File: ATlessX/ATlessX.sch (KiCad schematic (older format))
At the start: 13 parts, among them U1 74LS74, U2 74LS14

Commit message: More of the circuit done
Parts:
- gave numbers to parts that had none: 1
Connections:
- wire segments 12 -> 31
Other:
- moved on the sheet: C?, SW?, U2A
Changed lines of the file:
@@
 $Comp
 L 74xx:74LS14 U2
-U 1 1 5DD82518
-P 2500 2300
-F 0 "U2" H 2500 2617 50  0000 C CNN
-F 1 "74LS14" H 2500 2526 50  0000 C CNN
-F 2 "" H 2500 2300 50  0001 C CNN
-F 3 "http://www.ti.com/lit/gpn/sn74LS14" H 2500 2300 50  0001 C CNN
-	1    2500 2300
+U 2 1 5DD82518
+P 2650 3500
+F 0 "U2" H 2650 3817 50  0000 C CNN
+F 1 "74LS14" H 2650 3726 50  0000 C CNN
+F 2 "" H 2650 3500 50  0001 C CNN
+F 3 "http://www.ti.com/lit/gpn/sn74LS14" H 2650 3500 50  0001 C CNN
+	2    2650 3500
 	1    0    0    -1
 $EndComp
@@
 L Switch:SW_Push SW?
 U 1 1 5DD82728
-P 2250 3600
-F 0 "SW?" H 2250 3885 50  0000 C CNN
-F 1 "SW_Push" H 2250 3794 50  0000 C CNN
-F 2 "" H 2250 3800 50  0001 C CNN
-F 3 "~" H 2250 3800 50  0001 C CNN
-	1    2250 3600
-	1    0    0    -1
+P 850 3950
+F 0 "SW?" V 896 3902 50  0000 R CNN
+F 1 "SW_Push" V 805 3902 50  0000 R CNN
+F 2 "" H 850 4150 50  0001 C CNN
+F 3 "~" H 850 4150 50  0001 C CNN
+	1    850  3950
+	0    -1   -1   0
 $EndComp
 $Comp
 L Device:CP1_Small C?
 U 1 1 5DD82992
-P 2150 4400
-F 0 "C?" H 2241 4446 50  0000 L CNN
-F 1 "CP1_Small" H 2241 4355 50  0000 L CNN
-F 2 "" H 2150 4400 50  0001 C CNN
-F 3 "~" H 2150 4400 50  0001 C CNN
-	1    2150 4400
-	1    0    0    -1
-$EndComp
-$Comp
-L 74xx:74LS14 U?
+P 1950 4050
+F 0 "C?" H 2041 4096 50  0000 L CNN
+F 1 "CP1_Small" H 2041 4005 50  0000 L CNN
+F 2 "" H 1950 4050 50  0001 C CNN
+F 3 "~" H 1950 4050 50  0001 C CNN
+	1    1950 4050
+	1    0    0    -1
+$EndComp
+$Comp
+L 74xx:74LS14 U2
 U 1 1 5DD82CD4
-P 2900 1900
-F 0 "U?" H 2900 2217 50  0000 C CNN
-F 1 "74LS14" H 2900 2126 50  0000 C CNN
-F 2 "" H 2900 1900 50  0001 C CNN
-F 3 "http://www.ti.com/lit/gpn/sn74LS14" H 2900 1900 50  0001 C CNN
-	1    2900 1900
-	1    0    0    -1
-$EndComp
-$Comp
-L 74xx:74LS14 U?
-U 1 1 5DD82D12
-P 3250 2350
-F 0 "U?" H 3250 2667 50  0000 C CNN
-F 1 "74LS14" H 3250 2576 50  0000 C CNN
-F 2 "" H 3250 2350 50  0001 C CNN
-F 3 "http://www.ti.com/lit/gpn/sn74LS14" H 3250 2350 50  0001 C CNN
-	1    3250 2350
+P 3250 2850
+F 0 "U2" H 3250 3167 50  0000 C CNN
+F 1 "74LS14" H 3250 3076 50  0000 C CNN
+F 2 "" H 3250 2850 50  0001 C CNN
+F 3 "http://www.ti.com/lit/gpn/sn74LS14" H 3250 2850 50  0001 C CNN
+	1    3250 2850
+	1    0    0    -1
+$EndComp
+$Comp
+L 74xx:74LS14 U2
+U 3 1 5DD82D12
+P 3800 3500
+F 0 "U2" H 3800 3817 50  0000 C CNN
+F 1 "74LS14" H 3800 3726 50  0000 C CNN
+F 2 "" H 3800 3500 50  0001 C CNN
+F 3 "http://www.ti.com/lit/gpn/sn74LS14" H 3800 3500 50  0001 C CNN
+	3    3800 3500
 	1    0    0    -1
 $EndComp
@@
 L Device:CP1_Small C?
 U 1 1 5DD82E48
-P 1700 3950
-F 0 "C?" H 1791 3996 50  0000 L CNN
-F 1 "CP1_Small" H 1791 3905 50  0000 L CNN
-F 2 "" H 1700 3950 50  0001 C CNN
-F 3 "~" H 1700 3950 50  0001 C CNN
-	1    1700 3950
-	1    0    0    -1
-$EndComp
+P 1350 4050
+F 0 "C?" H 1441 4096 50  0000 L CNN
+F 1 "CP1_Small" H 1441 4005 50  0000 L CNN
+F 2 "" H 1350 4050 50  0001 C CNN
+F 3 "~" H 1350 4050 50  0001 C CNN
+	1    1350 4050
+	1    0    0    -1
+$EndComp
+Wire Wire Line
+	2950 3500 3500 3500
+Wire Wire Line
+	4100 3500 5100 3500
+Wire Wire Line
+	5100 3500 5100 2500
+Wire Wire Line
+	5100 2500 5700 2500
+Wire Wire Line
+	5700 2500 5700 2850
+Wire Wire Line
+	3550 2850 4700 2850
+Wire Wire Line
+	4700 2850 4700 3150
+Wire Wire Line
+	4700 3150 5400 3150
+Wire Wire Line
+	5400 3050 5250 3050
+Wire Wire Line
+	5250 3050 5250 3700
+Wire Wire Line
+	5250 3700 6200 3700
+Wire Wire Line
+	6200 3700 6200 3250
+Wire Wire Line
+	6200 3250 6000 3250
+Wire Wire Line
+	850  4150 850  4450
+Wire Wire Line
+	850  4450 1350 4450
+Wire Wire Line
+	1950 4450 1950 4150
+Wire Wire Line
+	1350 4150 1350 4450
+Connection ~ 1350 4450
+Wire Wire Line
+	1350 4450 1950 4450
+$Comp
+L power:GND #PWR?
+U 1 1 5DD84F2D
+P 1350 4750
+F 0 "#PWR?" H 1350 4500 50  0001 C CNN
+F 1 "GND" V 1355 4622 50  0000 R CNN
+F 2 "" H 1350 4750 50  0001 C CNN
+F 3 "" H 1350 4750 50  0001 C CNN
+	1    1350 4750
+	1    0    0    -1
+$EndComp
+Wire Wire Line
+	1350 4450 1350 4750
 $EndSCHEMATC

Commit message: Update schematic
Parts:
- C1: renamed from C?; value CP1_Small -> 1uF
- C2: renamed from C?; value CP1_Small -> 10uF
- D1, D2: renamed from D?; value D_Small -> 1N4148
- R1, R2: renamed from R?; value R_Small -> 10K
- R3: renamed from R?; value R_Small -> 470
- SW1: renamed from SW?; value SW_Push -> Power
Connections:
- net labels added: 5VSB, PWR_SW
- wire segments 31 -> 51
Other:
- note added: "ATX Power On Circuit"
- moved on the sheet: D1, D2, R1, R2, R3
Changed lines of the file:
@@
 F 3 "74xx/74hc_hct74.pdf" H 5600 1250 50  0001 C CNN
 	3    5600 1250
-	0    1    1    0
+	0    -1   1    0
 $EndComp
 $Comp
@@
 F 3 "http://www.ti.com/lit/gpn/sn74LS14" H 5600 1900 50  0001 C CNN
 	7    5600 1900
-	0    1    1    0
+	0    -1   1    0
 $EndComp
 Wire Wire Line
@@
 Connection ~ 5000 1900
 $Comp
-L Device:D_Small D?
+L Device:D_Small D1
 U 1 1 5DD82675
-P 1200 1450
-F 0 "D?" H 1200 1655 50  0000 C CNN
-F 1 "D_Small" H 1200 1564 50  0000 C CNN
-F 2 "" V 1200 1450 50  0001 C CNN
-F 3 "~" V 1200 1450 50  0001 C CNN
-	1    1200 1450
-	1    0    0    -1
-$EndComp
-$Comp
-L Device:R_Small R?
+P 1350 2350
+F 0 "D1" H 1350 2555 50  0000 C CNN
+F 1 "1N4148" H 1350 2464 50  0000 C CNN
+F 2 "" V 1350 2350 50  0001 C CNN
+F 3 "~" V 1350 2350 50  0001 C CNN
+	1    1350 2350
+	0    1    1    0
+$EndComp
+$Comp
+L Device:R_Small R3
 U 1 1 5DD827BB
-P 850 1800
-F 0 "R?" H 909 1846 50  0000 L CNN
-F 1 "R_Small" H 909 1755 50  0000 L CNN
-F 2 "" H 850 1800 50  0001 C CNN
-F 3 "~" H 850 1800 50  0001 C CNN
-	1    850  1800
-	1    0    0    -1
-$EndComp
-$Comp
-L Switch:SW_Push SW?
+P 1100 2850
+F 0 "R3" H 1159 2896 50  0000 L CNN
+F 1 "470" H 1159 2805 50  0000 L CNN
+F 2 "" H 1100 2850 50  0001 C CNN
+F 3 "~" H 1100 2850 50  0001 C CNN
+	1    1100 2850
+	0    1    1    0
+$EndComp
+$Comp
+L Switch:SW_Push SW1
 U 1 1 5DD82728
 P 850 3950
-F 0 "SW?" V 896 3902 50  0000 R CNN
-F 1 "SW_Push" V 805 3902 50  0000 R CNN
+F 0 "SW1" V 896 3902 50  0000 R CNN
+F 1 "Power" V 805 3902 50  0000 R CNN
 F 2 "" H 850 4150 50  0001 C CNN
 F 3 "~" H 850 4150 50  0001 C CNN
@@
 $EndComp
 $Comp
-L Device:CP1_Small C?
+L Device:CP1_Small C2
 U 1 1 5DD82992
 P 1950 4050
-F 0 "C?" H 2041 4096 50  0000 L CNN
-F 1 "CP1_Small" H 2041 4005 50  0000 L CNN
+F 0 "C2" H 2041 4096 50  0000 L CNN
+F 1 "10uF" H 2041 4005 50  0000 L CNN
 F 2 "" H 1950 4050 50  0001 C CNN
 F 3 "~" H 1950 4050 50  0001 C CNN
@@
 $EndComp
 $Comp
-L Device:R_Small R?
+L Device:R_Small R1
 U 1 1 5DD82D7E
-P 600 2150
-F 0 "R?" H 659 2196 50  0000 L CNN
-F 1 "R_Small" H 659 2105 50  0000 L CNN
-F 2 "" H 600 2150 50  0001 C CNN
-F 3 "~" H 600 2150 50  0001 C CNN
-	1    600  2150
-	1    0    0    -1
-$EndComp
-$Comp
-L Device:R_Small R?
+P 850 2350
+F 0 "R1" H 909 2396 50  0000 L CNN
+F 1 "10K" H 909 2305 50  0000 L CNN
+F 2 "" H 850 2350 50  0001 C CNN
+F 3 "~" H 850 2350 50  0001 C CNN
+	1    850  2350
+	1    0    0    -1
+$EndComp
+$Comp
+L Device:R_Small R2
 U 1 1 5DD82DBA
-P 1200 2250
-F 0 "R?" H 1259 2296 50  0000 L CNN
-F 1 "R_Small" H 1259 2205 50  0000 L CNN
-F 2 "" H 1200 2250 50  0001 C CNN
-F 3 "~" H 1200 2250 50  0001 C CNN
-	1    1200 2250
-	1    0    0    -1
-$EndComp
-$Comp
-L Device:D_Small D?
+P 1650 2350
+F 0 "R2" H 1709 2396 50  0000 L CNN
+F 1 "10K" H 1709 2305 50  0000 L CNN
+F 2 "" H 1650 2350 50  0001 C CNN
+F 3 "~" H 1650 2350 50  0001 C CNN
+	1    1650 2350
+	1    0    0    -1
+$EndComp
+$Comp
+L Device:D_Small D2
 U 1 1 5DD82DEF
-P 1700 1350
-F 0 "D?" H 1700 1555 50  0000 C CNN
-F 1 "D_Small" H 1700 1464 50  0000 C CNN
-F 2 "" V 1700 1350 50  0001 C CNN
-F 3 "~" V 1700 1350 50  0001 C CNN
-	1    1700 1350
-	1    0    0    -1
-$EndComp
-$Comp
-L Device:CP1_Small C?
+P 1950 2350
+F 0 "D2" H 1950 2555 50  0000 C CNN
+F 1 "1N4148" H 1950 2464 50  0000 C CNN
+F 2 "" V 1950 2350 50  0001 C CNN
+F 3 "~" V 1950 2350 50  0001 C CNN
+	1    1950 2350
+	0    1    1    0
+$EndComp
+$Comp
+L Device:CP1_Small C1
 U 1 1 5DD82E48
 P 1350 4050
-F 0 "C?" H 1441 4096 50  0000 L CNN
-F 1 "CP1_Small" H 1441 4005 50  0000 L CNN
+F 0 "C1" H 1441 4096 50  0000 L CNN
+F 1 "1uF" H 1441 4005 50  0000 L CNN
 F 2 "" H 1350 4050 50  0001 C CNN
 F 3 "~" H 1350 4050 50  0001 C CNN
@@
 Wire Wire Line
 	1350 4450 1350 4750
+Wire Wire Line
+	1650 2450 1650 3500
+Wire Wire Line
+	1650 3500 1950 3500
+Wire Wire Line
+	1950 3950 1950 3500
+Connection ~ 1950 3500
+Wire Wire Line
+	1950 3500 2350 3500
+Wire Wire Line
+	1950 3500 1950 2450
+Wire Wire Line
+	1350 2450 1350 2850
+Wire Wire Line
+	2950 2850 1350 2850
+Connection ~ 1350 2850
+Wire Wire Line
+	1350 2850 1350 3950
+Wire Wire Line
+	1200 2850 1350 2850
+Wire Wire Line
+	850  3750 850  2850
+Wire Wire Line
+	850  2850 1000 2850
+Wire Wire Line
+	850  2850 850  2450
+Connection ~ 850  2850
+Wire Wire Line
+	850  2250 850  1900
+Wire Wire Line
+	850  1900 1350 1900
+Wire Wire Line
+	1950 2250 1950 1900
+Connection ~ 1950 1900
+Wire Wire Line
+	1950 1900 5000 1900
+Wire Wire Line
+	1650 2250 1650 1900
+Connection ~ 1650 1900
+Wire Wire Line
+	1650 1900 1950 1900
+Wire Wire Line
+	1350 2250 1350 1900
+Connection ~ 1350 1900
+Wire Wire Line
+	1350 1900 1650 1900
+Text Label 900  1900 0    50   ~ 0
+5VSB
+Text Label 850  3400 1    50   ~ 0
+PWR_SW
+Wire Notes Line
+	650  650  6950 650
+Wire Notes Line
+	6950 650  6950 5100
+Wire Notes Line
+	6950 5100 650  5100
+Wire Notes Line
+	650  5100 650  650
+Text Notes 6800 5000 2    168  ~ 0
+ATX Power On Circuit
 $EndSCHEMATC

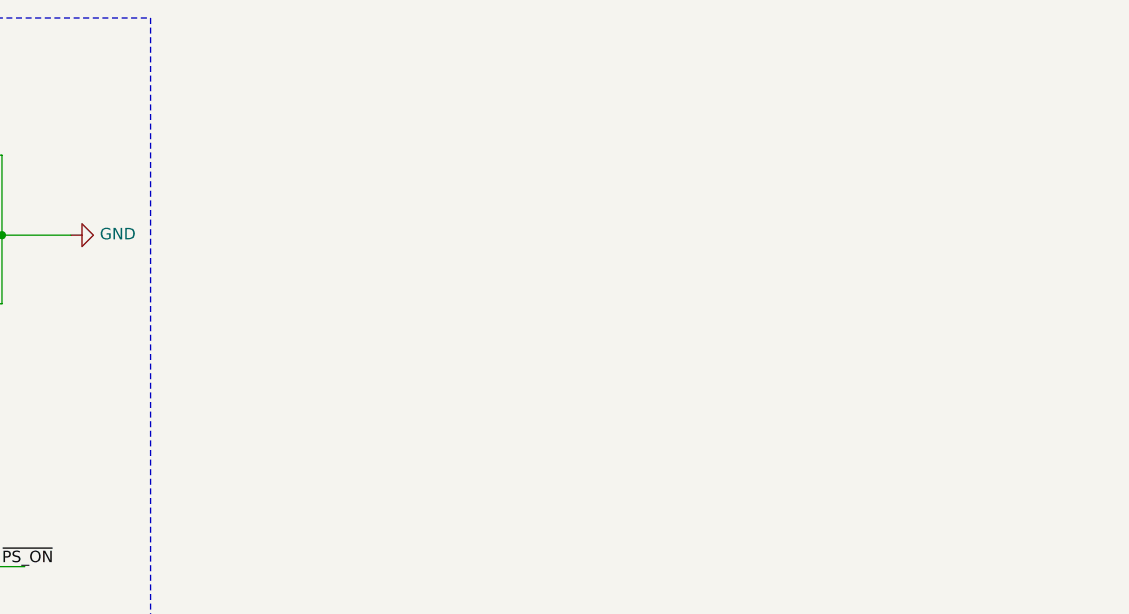
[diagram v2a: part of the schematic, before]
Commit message: Add power leds
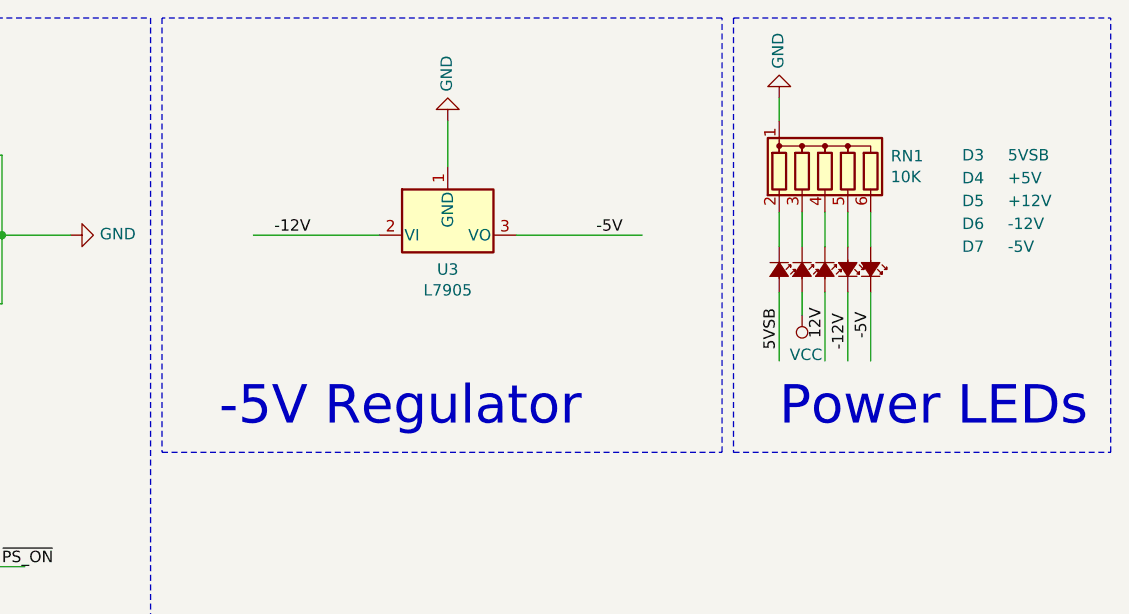
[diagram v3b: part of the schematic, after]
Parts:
- added D3: 5VSB, symbol Device:LED_Small_ALT
- added D4: +5V, symbol Device:LED_Small_ALT
- added D5: +12V, symbol Device:LED_Small_ALT
- added D6: -12V, symbol Device:LED_Small_ALT
- added D7: -5V, symbol Device:LED_Small_ALT
- added RN1: 10K, Resistor_THT:R_Array_SIP6, symbol Device:R_Network05
- added U3: L7905, symbol Regulator_Linear:L7905
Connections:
- net labels added: -12V, -5V, 12V, VCC
- wire segments 51 -> 65
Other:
- note added: "-5V Regulator"
- note added: "Power LEDs"
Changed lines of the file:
@@
 Text Notes 6800 5000 2    168  ~ 0
 ATX Power On Circuit
+$Comp
+L Regulator_Linear:L7905 U3
+U 1 1 5DDA03DD
+P 8250 1600
+F 0 "U3" H 8250 1450 50  0000 C CNN
+F 1 "L7905" H 8250 1359 50  0000 C CNN
+F 2 "" H 8250 1400 50  0001 C CIN
+F 3 "http://www.st.com/content/ccc/resource/technical/document/datasheet/c9/16/86/41/c7/2b/45/f2/CD00000450.pdf/files/CD00000450.pdf/jcr:content/translations/en.CD00000450.pdf" H 8250 1600 50  0001 C CNN
+	1    8250 1600
+	1    0    0    -1
+$EndComp
+$Comp
+L power:GND #PWR?
+U 1 1 5DDA0489
+P 8250 1100
+F 0 "#PWR?" H 8250 850 50  0001 C CNN
+F 1 "GND" V 8255 972 50  0000 R CNN
+F 2 "" H 8250 1100 50  0001 C CNN
+F 3 "" H 8250 1100 50  0001 C CNN
+	1    8250 1100
+	-1   0    0    1
+$EndComp
+Wire Wire Line
+	8250 1300 8250 1100
+Wire Wire Line
+	7950 1600 7400 1600
+Wire Wire Line
+	8550 1600 9100 1600
+Text Label 7650 1600 2    50   ~ 0
+-12V
+Text Label 8900 1600 0    50   ~ 0
+-5V
+Wire Notes Line
+	7000 650  7000 2550
+Wire Notes Line
+	7000 2550 9450 2550
+Wire Notes Line
+	9450 2550 9450 650
+Wire Notes Line
+	9450 650  7000 650
+Text Notes 7250 2450 0    168  ~ 0
+-5V Regulator
+$Comp
+L power:GND #PWR?
+U 1 1 5DDA6B94
+P 9700 1000
+F 0 "#PWR?" H 9700 750 50  0001 C CNN
+F 1 "GND" V 9705 872 50  0000 R CNN
+F 2 "" H 9700 1000 50  0001 C CNN
+F 3 "" H 9700 1000 50  0001 C CNN
+	1    9700 1000
+	-1   0    0    1
+$EndComp
+Wire Wire Line
+	9700 1000 9700 1100
+$Comp
+L Device:R_Network05 RN1
+U 1 1 5DDA9E15
+P 9900 1300
+F 0 "RN1" H 10188 1346 50  0000 L CNN
+F 1 "10K" H 10188 1255 50  0000 L CNN
+F 2 "Resistor_THT:R_Array_SIP6" V 10275 1300 50  0001 C CNN
+F 3 "http://www.vishay.com/docs/31509/csc.pdf" H 9900 1300 50  0001 C CNN
+	1    9900 1300
+	1    0    0    -1
+$EndComp
+$Comp
+L Device:LED_Small_ALT D3
+U 1 1 5DDAAF5F
+P 9700 1750
+F 0 "D3" V 9200 2550 50  0000 L CNN
+F 1 "5VSB" V 9200 2750 50  0000 L CNN
+F 2 "" V 9700 1750 50  0001 C CNN
+F 3 "~" V 9700 1750 50  0001 C CNN
+	1    9700 1750
+	0    1    1    0
+$EndComp
+$Comp
+L Device:LED_Small_ALT D4
+U 1 1 5DDAC147
+P 9800 1750
+F 0 "D4" V 9400 2450 50  0000 L CNN
+F 1 "+5V" V 9400 2650 50  0000 L CNN
+F 2 "" V 9800 1750 50  0001 C CNN
+F 3 "~" V 9800 1750 50  0001 C CNN
+	1    9800 1750
+	0    1    1    0
+$EndComp
+$Comp
+L Device:LED_Small_ALT D5
+U 1 1 5DDAC1AF
+P 9900 1750
+F 0 "D5" V 9600 2350 50  0000 L CNN
+F 1 "+12V" V 9600 2550 50  0000 L CNN
+F 2 "" V 9900 1750 50  0001 C CNN
+F 3 "~" V 9900 1750 50  0001 C CNN
+	1    9900 1750
+	0    1    1    0
+$EndComp
+$Comp
+L Device:LED_Small_ALT D6
+U 1 1 5DDAC207
+P 10000 1750
+F 0 "D6" V 10200 2250 50  0000 L CNN
+F 1 "-12V" V 10200 2450 50  0000 L CNN
+F 2 "" V 10000 1750 50  0001 C CNN
+F 3 "~" V 10000 1750 50  0001 C CNN
+	1    10000 1750
+	0    1    -1   0
+$EndComp
+$Comp
+L Device:LED_Small_ALT D7
+U 1 1 5DDAD244
+P 10100 1750
+F 0 "D7" V 10200 2150 50  0000 L CNN
+F 1 "-5V" V 10200 2350 50  0000 L CNN
+F 2 "" V 10100 1750 50  0001 C CNN
+F 3 "~" V 10100 1750 50  0001 C CNN
+	1    10100 1750
+	0    1    -1   0
+$EndComp
+Wire Wire Line
+	10100 1500 10100 1650
+Wire Wire Line
+	10000 1500 10000 1650
+Wire Wire Line
+	9900 1500 9900 1650
+Wire Wire Line
+	9800 1500 9800 1650
+Wire Wire Line
+	9700 1500 9700 1650
+Wire Wire Line
+	9700 1850 9700 2150
+$Comp
+L power:VCC #PWR?
+U 1 1 5DDB34E7
+P 9800 1950
+F 0 "#PWR?" H 9800 1800 50  0001 C CNN
+F 1 "VCC" H 9817 2123 50  0000 C CNN
+F 2 "" H 9800 1950 50  0001 C CNN
+F 3 "" H 9800 1950 50  0001 C CNN
+	1    9800 1950
+	1    0    0    1
+$EndComp
+Wire Wire Line
+	9800 1850 9800 1950
+Wire Wire Line
+	9900 1850 9900 2150
+Wire Wire Line
+	10000 1850 10000 2150
+Wire Wire Line
+	10100 1850 10100 2150
+Text Label 9700 2100 1    50   ~ 0
+5VSB
+Text Label 9900 2050 1    50   ~ 0
+12V
+Text Label 10000 2100 1    50   ~ 0
+-12V
+Text Label 10100 2050 1    50   ~ 0
+-5V
+Wire Notes Line
+	11150 2550 11150 650
+Wire Notes Line
+	9500 650  9500 2550
+Wire Notes Line
+	9500 2550 11150 2550
+Wire Notes Line
+	9500 650  11150 650
+Text Notes 11050 2450 2    168  ~ 0
+Power LEDs
 $EndSCHEMATC

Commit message: First draft of the schematic
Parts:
- added J1: EXT_PWR_SW, symbol Connector:Conn_01x02_Male
- added J2: ATX, symbol Connector_Generic:Conn_02x10_Top_Bottom
- added J3: P8, symbol Connector:Conn_01x06_Male
- added J4: P9, symbol Connector:Conn_01x06_Male
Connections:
- net labels added: +12V, PWR_OK
- wire segments 65 -> 119
- no-connect marks 0 -> 4
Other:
- note added: "AT Connectors"
- note added: "ATX Connector"

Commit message: Fix error
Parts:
- gave numbers to parts that had none: 1
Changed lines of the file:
@@
 $EndComp
 $Comp
-L 74xx:74LS74 U?
+L 74xx:74LS74 U1
 U 1 1 5DD823EB
 P 5700 3150
-F 0 "U?" H 5700 3628 50  0000 C CNN
+F 0 "U1" H 5700 3628 50  0000 C CNN
 F 1 "74LS74" H 5700 3537 50  0000 C CNN
 F 2 "" H 5700 3150 50  0001 C CNN
